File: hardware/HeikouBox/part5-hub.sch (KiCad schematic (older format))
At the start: 51 parts, among them J501 Micro_SD_Card_TFP09-2-12B, J503 PS/2, Q502 BSS138, Q503 BSS138, SW501 Left, SW502 Right, SW503 Up, SW504 Down, U501 STM32-BluePill-Socket

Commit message: BOM reduction
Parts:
- R524, R529: value 100R -> 1K
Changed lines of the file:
@@
 AR Path="/63C0F973" Ref="R?"  Part="1"
 AR Path="/646E3FCF/63C0F973" Ref="R529"  Part="1"
-F 0 "R529" V 7750 2800 50  0000 C CNN
-F 1 "100R" V 7650 2800 50  0000 C CNN
+F 0 "R529" V 7550 2800 50  0000 C CNN
+F 1 "1K" V 7650 2800 50  0000 C CNN
 F 2 "Resistor_SMD:R_0603_1608Metric_Pad0.98x0.95mm_HandSolder" V 7580 2800 50  0001 C CNN
 F 3 "~" H 7650 2800 50  0001 C CNN
@@
 AR Path="/646E3FCF/63BFC404" Ref="R524"  Part="1"
 F 0 "R524" V 7750 2600 50  0000 C CNN
-F 1 "100R" V 7650 2600 50  0000 C CNN
+F 1 "1K" V 7650 2600 50  0000 C CNN
 F 2 "Resistor_SMD:R_0603_1608Metric_Pad0.98x0.95mm_HandSolder" V 7580 2600 50  0001 C CNN
 F 3 "~" H 7650 2600 50  0001 C CNN

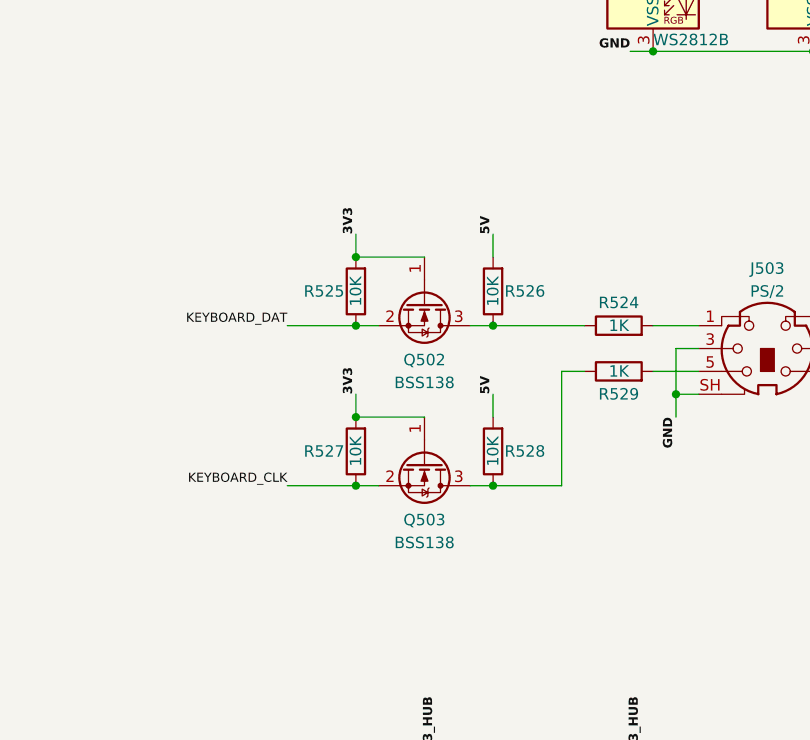
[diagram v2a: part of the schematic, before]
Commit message: Shrink VGA ladders to make space for xbus redo
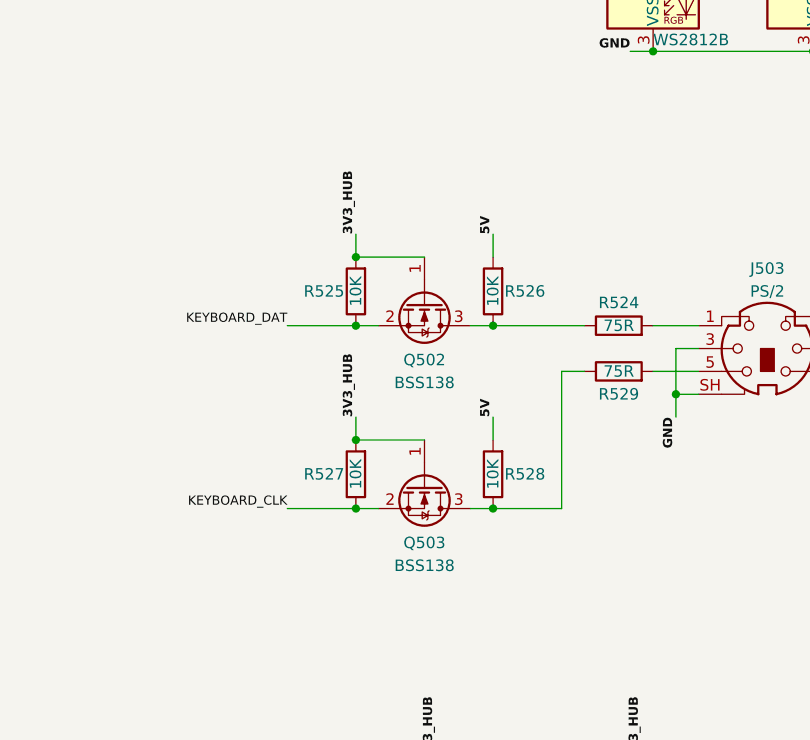
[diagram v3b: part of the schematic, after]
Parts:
- R524, R529: value 1K -> 75R
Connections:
- net 3V3: no longer Q502.1 (G), Q503.1 (G), R525.2, R527.2
- net 3V3_HUB: now also Q502.1 (G), Q503.1 (G), R525.2, R527.2
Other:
- moved on the sheet: Q503, R527, R528
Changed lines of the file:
@@
 Wire Wire Line
 	6200 2600 6500 2600
-Text Label 6200 3300 2    40   ~ 0
+Text Label 6200 3400 2    40   ~ 0
 KEYBOARD_CLK
 Wire Wire Line
@@
 Connection ~ 6500 2300
 Wire Wire Line
-	6500 3300 6200 3300
+	6500 3400 6200 3400
 Connection ~ 6500 2600
-Connection ~ 6500 3300
-Connection ~ 6500 3000
-Wire Wire Line
-	6500 3000 6500 2900
-Wire Wire Line
-	6500 3300 6600 3300
-Wire Wire Line
-	6500 3000 6800 3000
+Connection ~ 6500 3400
+Connection ~ 6500 3100
+Wire Wire Line
+	6500 3100 6500 3000
+Wire Wire Line
+	6500 3400 6600 3400
+Wire Wire Line
+	6500 3100 6800 3100
 $Comp
 L Device:R R?
 U 1 1 637DC681
-P 6500 3150
+P 6500 3250
 AR Path="/637DC681" Ref="R?"  Part="1"
 AR Path="/646E3FCF/637DC681" Ref="R527"  Part="1"
-F 0 "R527" H 6550 3150 50  0000 L CNN
-F 1 "10K" V 6500 3150 50  0000 C CNN
-F 2 "Resistor_SMD:R_0603_1608Metric_Pad0.98x0.95mm_HandSolder" V 6430 3150 50  0001 C CNN
-F 3 "~" H 6500 3150 50  0001 C CNN
-	1    6500 3150
+F 0 "R527" H 6550 3250 50  0000 L CNN
+F 1 "10K" V 6500 3250 50  0000 C CNN
+F 2 "Resistor_SMD:R_0603_1608Metric_Pad0.98x0.95mm_HandSolder" V 6430 3250 50  0001 C CNN
+F 3 "~" H 6500 3250 50  0001 C CNN
+	1    6500 3250
 	-1   0    0    1
 $EndComp
@@
 L Transistor_FET:BSS138 Q503
 U 1 1 637DC67B
-P 6800 3200
-F 0 "Q503" V 7050 3200 50  0000 C CNN
-F 1 "BSS138" V 7150 3200 50  0000 C CNN
-F 2 "Package_TO_SOT_SMD:SOT-23" H 7000 3125 50  0001 L CIN
-F 3 "https://www.onsemi.com/pub/Collateral/BSS138-D.PDF" H 6800 3200 50  0001 L CNN
-	1    6800 3200
+P 6800 3300
+F 0 "Q503" V 7050 3300 50  0000 C CNN
+F 1 "BSS138" V 7150 3300 50  0000 C CNN
+F 2 "Package_TO_SOT_SMD:SOT-23" H 7000 3225 50  0001 L CIN
+F 3 "https://www.onsemi.com/pub/Collateral/BSS138-D.PDF" H 6800 3300 50  0001 L CNN
+	1    6800 3300
 	0    1    1    0
 $EndComp
@@
 	7500 2800 7400 2800
 Wire Wire Line
-	7400 2800 7400 3300
-Connection ~ 7100 3300
-Wire Wire Line
-	7400 3300 7100 3300
-Wire Wire Line
-	7100 3300 7000 3300
+	7400 2800 7400 3400
+Connection ~ 7100 3400
+Wire Wire Line
+	7400 3400 7100 3400
+Wire Wire Line
+	7100 3400 7000 3400
 $Comp
 L Device:R R?
 U 1 1 637DC687
-P 7100 3150
+P 7100 3250
 AR Path="/637DC687" Ref="R?"  Part="1"
 AR Path="/646E3FCF/637DC687" Ref="R528"  Part="1"
-F 0 "R528" H 7050 3150 50  0000 R CNN
-F 1 "10K" V 7100 3150 50  0000 C CNN
-F 2 "Resistor_SMD:R_0603_1608Metric_Pad0.98x0.95mm_HandSolder" V 7030 3150 50  0001 C CNN
-F 3 "~" H 7100 3150 50  0001 C CNN
-	1    7100 3150
+F 0 "R528" H 7050 3250 50  0000 R CNN
+F 1 "10K" V 7100 3250 50  0000 C CNN
+F 2 "Resistor_SMD:R_0603_1608Metric_Pad0.98x0.95mm_HandSolder" V 7030 3250 50  0001 C CNN
+F 3 "~" H 7100 3250 50  0001 C CNN
+	1    7100 3250
 	-1   0    0    1
 $EndComp
@@
 $EndComp
 Wire Wire Line
-	7100 3000 7100 2900
+	7100 3100 7100 3000
 Wire Wire Line
 	7100 2300 7100 2200
@@
 AR Path="/646E3FCF/63C0F973" Ref="R529"  Part="1"
 F 0 "R529" V 7550 2800 50  0000 C CNN
-F 1 "1K" V 7650 2800 50  0000 C CNN
+F 1 "75R" V 7650 2800 50  0000 C CNN
 F 2 "Resistor_SMD:R_0603_1608Metric_Pad0.98x0.95mm_HandSolder" V 7580 2800 50  0001 C CNN
 F 3 "~" H 7650 2800 50  0001 C CNN
@@
 AR Path="/646E3FCF/63BFC404" Ref="R524"  Part="1"
 F 0 "R524" V 7750 2600 50  0000 C CNN
-F 1 "1K" V 7650 2600 50  0000 C CNN
+F 1 "75R" V 7650 2600 50  0000 C CNN
 F 2 "Resistor_SMD:R_0603_1608Metric_Pad0.98x0.95mm_HandSolder" V 7580 2600 50  0001 C CNN
 F 3 "~" H 7650 2600 50  0001 C CNN
@@
 Text Label 850  7600 0    40   ~ 8
 3V3
-Text Label 6500 2200 1    40   ~ 8
-3V3
-Text Label 6500 2900 1    40   ~ 8
-3V3
 Wire Wire Line
 	850  7500 750  7500
@@
 Text Label 850  7500 0    40   ~ 8
 5V
-Text Label 7100 2900 1    40   ~ 8
+Text Label 7100 3000 1    40   ~ 8
 5V
 Text Label 7100 2200 1    40   ~ 8
@@
 Text Notes 2750 2300 0    40   ~ 0
 to resistor fix
+Text Label 6500 3000 1    40   ~ 8
+3V3_HUB
+Text Label 6500 2200 1    40   ~ 8
+3V3_HUB
 Wire Bus Line
 	4700 6900 4700 7700

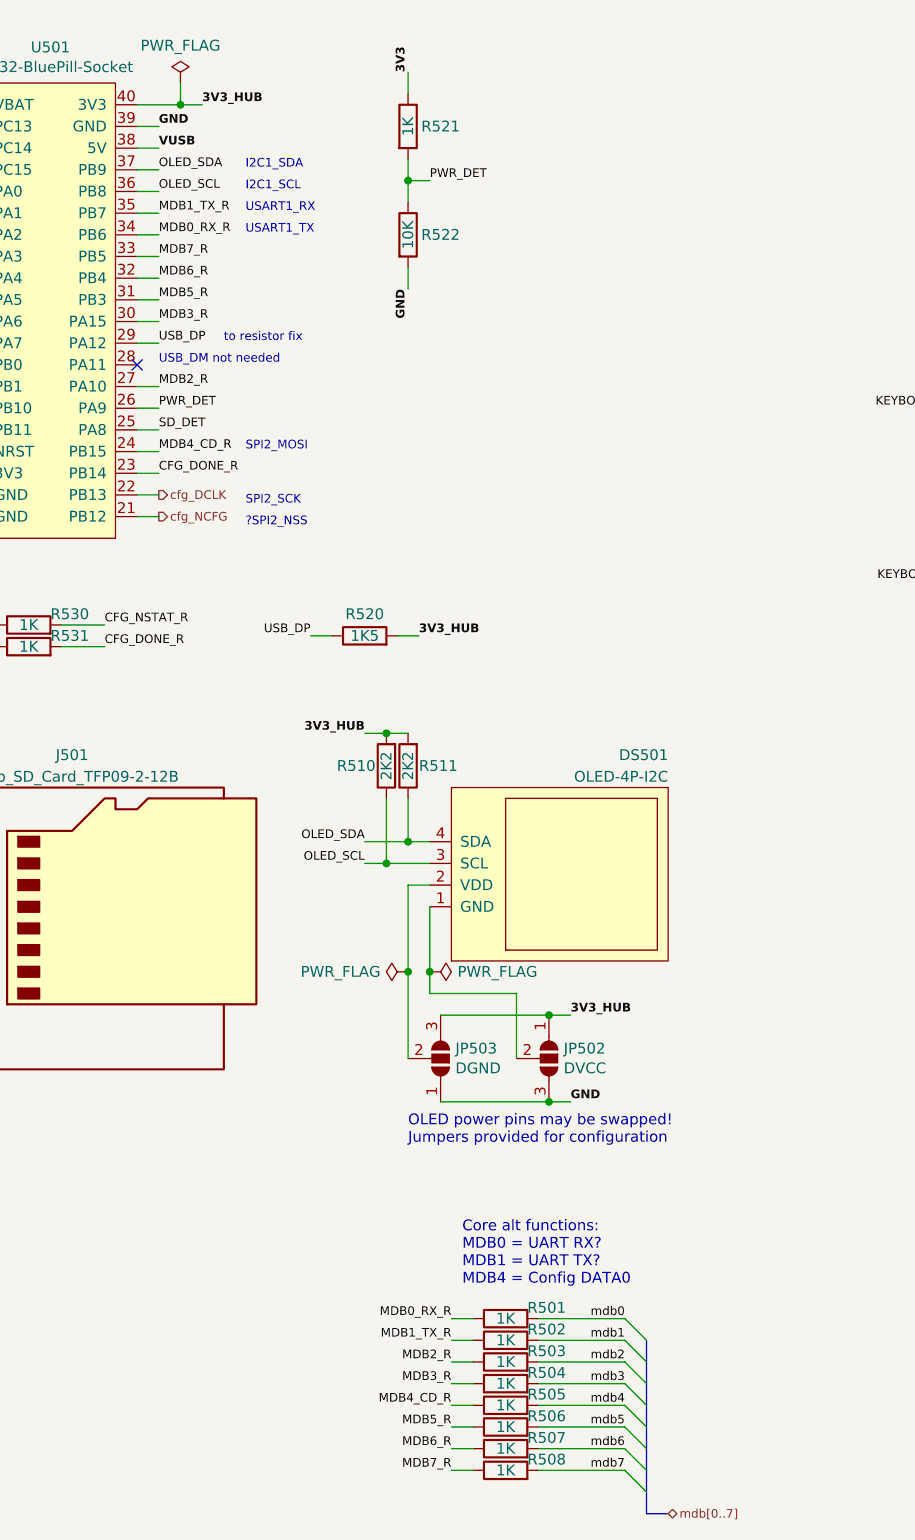
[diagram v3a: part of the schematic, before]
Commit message: Connect UART correctly, remove unused mdb connection & mdb terminology
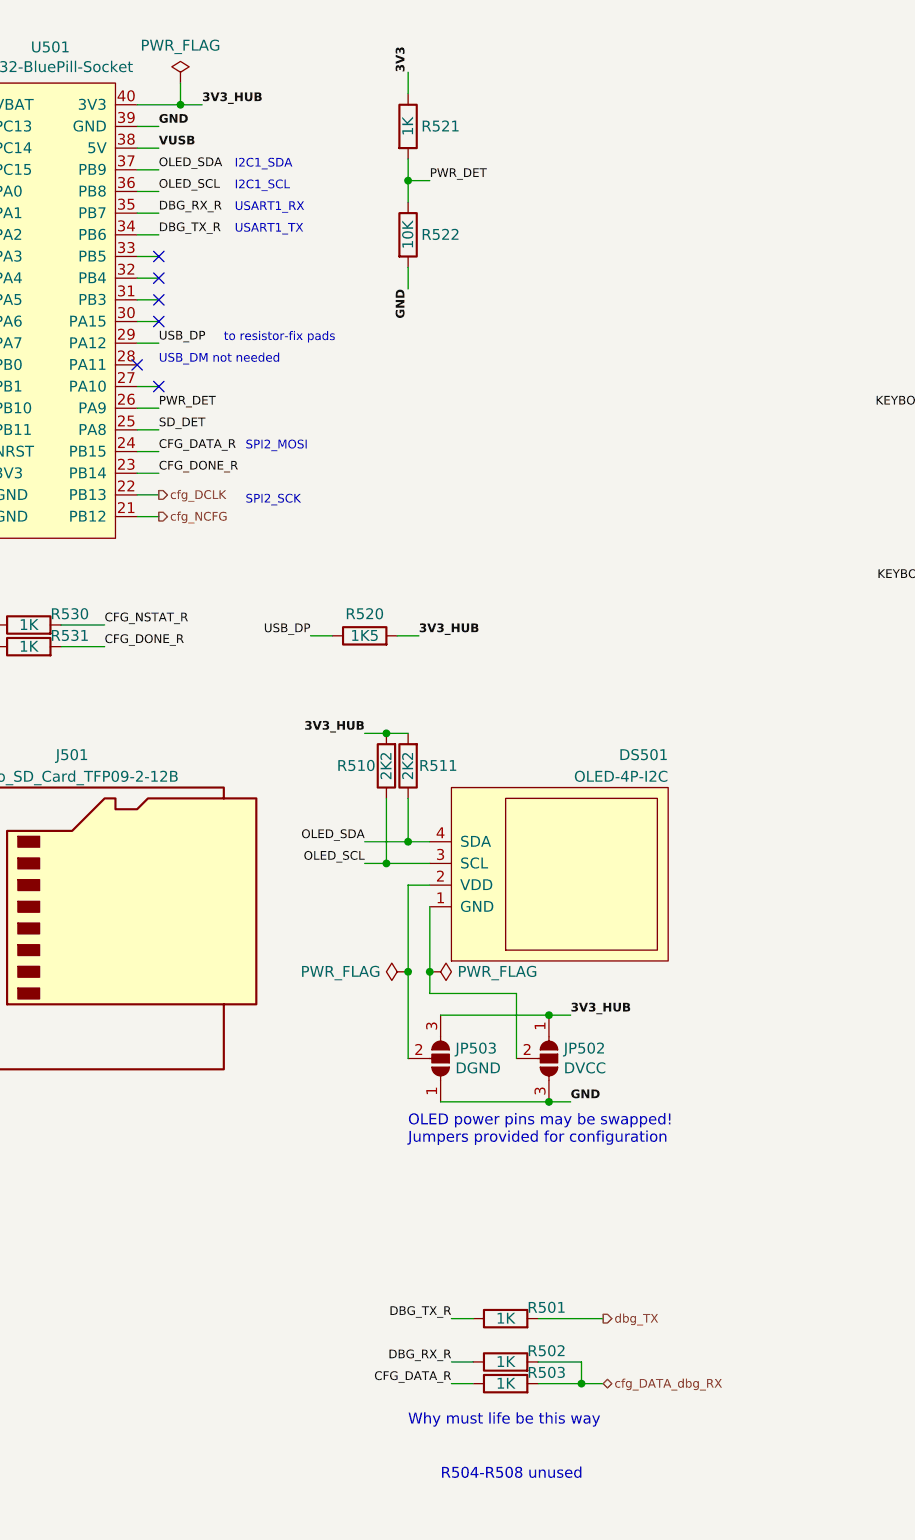
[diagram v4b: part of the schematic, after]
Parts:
- removed R504, R505, R506, R507, R508: 1K, Resistor_SMD:R_0603_1608Metric_Pad0.98x0.95mm_HandSolder, symbol Device:R
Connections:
- net mdb2 is gone; now on net cfg_DATA_dbg_RX: R503.2
- net MDB0_RX_R renamed DBG_TX_R
- net MDB1_TX_R renamed DBG_RX_R
- net MDB2_R: no longer names the net of U501.27 (PA10)
- net MDB2_R: no longer R503.1
- net MDB3_R: no longer names the net of U501.30 (PA15)
- net MDB4_CD_R renamed CFG_DATA_R
- net CFG_DATA_R: now also R503.1
- net MDB5_R: no longer names the net of U501.31 (PB3)
- net MDB6_R: no longer names the net of U501.32 (PB4)
- net MDB7_R: no longer names the net of U501.33 (PB5)
- net mdb0 renamed dbg_TX
- net mdb1 renamed cfg_DATA_dbg_RX
- no-connect marks 12 -> 17
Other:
- note added: "R504-R508 unused"
- note added: "Why must life be this way"
- note added: "to resistor-fix pads"
- note removed: "?SPI2_NSS"
- note removed: "Core alt functions:\nMDB0 = UART RX?\nMDB1 = UART TX?\nMDB4 = Config DATA0"
- note removed: "to resistor fix"
- moved on the sheet: R502, R503
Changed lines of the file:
@@
 	1100 4700 1000 4700
-Wire Wire Line
-	4200 7100 4600 7100
-$Comp
-L Device:R R?
-U 1 1 63231DEC
-P 4050 7100
-AR Path="/63231DEC" Ref="R?"  Part="1"
-AR Path="/646E3FCF/63231DEC" Ref="R504"  Part="1"
-F 0 "R504" V 4100 7000 50  0000 R CNN
-F 1 "1K" V 4050 7100 50  0000 C CNN
-F 2 "Resistor_SMD:R_0603_1608Metric_Pad0.98x0.95mm_HandSolder" V 3980 7100 50  0001 C CNN
-F 3 "~" H 4050 7100 50  0001 C CNN
-	1    4050 7100
-	0    -1   -1   0
-$EndComp
-Entry Wire Line
-	4600 7100 4700 7200
-Entry Wire Line
-	4600 7400 4700 7500
-Entry Wire Line
-	4600 7500 4700 7600
-Wire Wire Line
-	4200 7400 4600 7400
-$Comp
-L Device:R R?
-U 1 1 6323C22A
-P 4050 7400
-AR Path="/6323C22A" Ref="R?"  Part="1"
-AR Path="/646E3FCF/6323C22A" Ref="R507"  Part="1"
-F 0 "R507" V 4100 7300 50  0000 R CNN
-F 1 "1K" V 4050 7400 50  0000 C CNN
-F 2 "Resistor_SMD:R_0603_1608Metric_Pad0.98x0.95mm_HandSolder" V 3980 7400 50  0001 C CNN
-F 3 "~" H 4050 7400 50  0001 C CNN
-	1    4050 7400
-	0    -1   -1   0
-$EndComp
 Wire Wire Line
 	1100 4700 1200 4700
@@
 Text HLabel 1600 3600 0    40   Input ~ 0
 cfg_NSTAT
-Entry Wire Line
-	4600 6800 4700 6900
-Wire Wire Line
-	4200 6900 4600 6900
-Wire Wire Line
-	4200 6800 4600 6800
 $Comp
 L Device:R R?
 U 1 1 63192B13
-P 4050 6900
+P 4050 7000
 AR Path="/63192B13" Ref="R?"  Part="1"
 AR Path="/646E3FCF/63192B13" Ref="R502"  Part="1"
-F 0 "R502" V 4100 6800 50  0000 R CNN
-F 1 "1K" V 4050 6900 50  0000 C CNN
-F 2 "Resistor_SMD:R_0603_1608Metric_Pad0.98x0.95mm_HandSolder" V 3980 6900 50  0001 C CNN
-F 3 "~" H 4050 6900 50  0001 C CNN
-	1    4050 6900
+F 0 "R502" V 4100 6900 50  0000 R CNN
+F 1 "1K" V 4050 7000 50  0000 C CNN
+F 2 "Resistor_SMD:R_0603_1608Metric_Pad0.98x0.95mm_HandSolder" V 3980 7000 50  0001 C CNN
+F 3 "~" H 4050 7000 50  0001 C CNN
+	1    4050 7000
 	0    -1   -1   0
 $EndComp
@@
 	0    -1   -1   0
 $EndComp
-Entry Wire Line
-	4600 6900 4700 7000
-$Comp
-L Device:R R?
-U 1 1 632371E8
-P 4050 7300
-AR Path="/632371E8" Ref="R?"  Part="1"
-AR Path="/646E3FCF/632371E8" Ref="R506"  Part="1"
-F 0 "R506" V 4100 7200 50  0000 R CNN
-F 1 "1K" V 4050 7300 50  0000 C CNN
-F 2 "Resistor_SMD:R_0603_1608Metric_Pad0.98x0.95mm_HandSolder" V 3980 7300 50  0001 C CNN
-F 3 "~" H 4050 7300 50  0001 C CNN
-	1    4050 7300
-	0    -1   -1   0
-$EndComp
-Wire Wire Line
-	4200 7300 4600 7300
-Entry Wire Line
-	4600 7300 4700 7400
-Entry Wire Line
-	4600 7200 4700 7300
-Wire Wire Line
-	4200 7200 4600 7200
-Entry Wire Line
-	4600 7000 4700 7100
-Wire Bus Line
-	4700 7700 4800 7700
-Wire Wire Line
-	4200 7000 4600 7000
+Wire Wire Line
+	4200 7100 4400 7100
 $Comp
 L Device:R R?
 U 1 1 63231DF2
-P 4050 7000
+P 4050 7100
 AR Path="/63231DF2" Ref="R?"  Part="1"
 AR Path="/646E3FCF/63231DF2" Ref="R503"  Part="1"
-F 0 "R503" V 4100 6900 50  0000 R CNN
-F 1 "1K" V 4050 7000 50  0000 C CNN
-F 2 "Resistor_SMD:R_0603_1608Metric_Pad0.98x0.95mm_HandSolder" V 3980 7000 50  0001 C CNN
-F 3 "~" H 4050 7000 50  0001 C CNN
-	1    4050 7000
-	0    -1   -1   0
-$EndComp
-$Comp
-L Device:R R?
-U 1 1 632371EE
-P 4050 7200
-AR Path="/632371EE" Ref="R?"  Part="1"
-AR Path="/646E3FCF/632371EE" Ref="R505"  Part="1"
-F 0 "R505" V 4100 7100 50  0000 R CNN
-F 1 "1K" V 4050 7200 50  0000 C CNN
-F 2 "Resistor_SMD:R_0603_1608Metric_Pad0.98x0.95mm_HandSolder" V 3980 7200 50  0001 C CNN
-F 3 "~" H 4050 7200 50  0001 C CNN
-	1    4050 7200
+F 0 "R503" V 4100 7000 50  0000 R CNN
+F 1 "1K" V 4050 7100 50  0000 C CNN
+F 2 "Resistor_SMD:R_0603_1608Metric_Pad0.98x0.95mm_HandSolder" V 3980 7100 50  0001 C CNN
+F 3 "~" H 4050 7100 50  0001 C CNN
+	1    4050 7100
 	0    -1   -1   0
 $EndComp
 Text HLabel 2450 3000 2    40   Output ~ 0
 cfg_DCLK
-Text HLabel 4800 7700 2    40   BiDi ~ 0
-mdb[0..7]
 $Comp
 L Device:R R?
@@
 Wire Wire Line
 	2200 3600 2000 3600
-Text Label 4600 7200 2    40   ~ 0
-mdb4
-Text Label 4600 7000 2    40   ~ 0
-mdb2
-Text Label 4600 7300 2    40   ~ 0
-mdb5
-Text Label 4600 6900 2    40   ~ 0
-mdb1
-Text Label 4600 6800 2    40   ~ 0
-mdb0
-Text Label 4600 7400 2    40   ~ 0
-mdb6
-Text Label 4600 7500 2    40   ~ 0
-mdb7
-Text Label 4600 7100 2    40   ~ 0
-mdb3
 Wire Wire Line
 	3400 4700 3500 4700
-Wire Wire Line
-	4200 7500 4600 7500
-$Comp
-L Device:R R?
-U 1 1 6323C224
-P 4050 7500
-AR Path="/6323C224" Ref="R?"  Part="1"
-AR Path="/646E3FCF/6323C224" Ref="R508"  Part="1"
-F 0 "R508" V 4100 7400 50  0000 R CNN
-F 1 "1K" V 4050 7500 50  0000 C CNN
-F 2 "Resistor_SMD:R_0603_1608Metric_Pad0.98x0.95mm_HandSolder" V 3980 7500 50  0001 C CNN
-F 3 "~" H 4050 7500 50  0001 C CNN
-	1    4050 7500
-	0    -1   -1   0
-$EndComp
 Wire Wire Line
 	7700 800  7800 800
@@
 Text Label 1000 4800 2    40   ~ 0
 SD_MOSI
-Text Label 3800 6900 2    40   ~ 0
-MDB1_TX_R
-Wire Wire Line
-	3800 6900 3900 6900
+Text Label 3800 7000 2    40   ~ 0
+DBG_RX_R
+Wire Wire Line
+	3800 7000 3900 7000
 Text Label 3800 6800 2    40   ~ 0
-MDB0_RX_R
+DBG_TX_R
 Wire Wire Line
 	3800 6800 3900 6800
-Text Label 3800 7200 2    40   ~ 0
-MDB4_CD_R
-Wire Wire Line
-	3800 7200 3900 7200
-Text Label 3800 7000 2    40   ~ 0
-MDB2_R
-Wire Wire Line
-	3800 7000 3900 7000
 Text Label 3800 7100 2    40   ~ 0
-MDB3_R
-Wire Wire Line
-	3800 7100 3900 7100
-Text Notes 3850 6650 0    50   ~ 0
-Core alt functions:\nMDB0 = UART RX?\nMDB1 = UART TX?\nMDB4 = Config DATA0
-Text Label 3800 7300 2    40   ~ 0
-MDB5_R
-Wire Wire Line
-	3800 7300 3900 7300
-Text Label 3800 7400 2    40   ~ 0
-MDB6_R
-Wire Wire Line
-	3800 7400 3900 7400
-Text Label 3800 7500 2    40   ~ 0
-MDB7_R
-Wire Wire Line
-	3800 7500 3900 7500
+CFG_DATA_R
 Wire Wire Line
 	6950 4900 6850 4900
@@
 Wire Wire Line
 	2450 2200 2350 2200
-Text Label 2450 2200 0    40   ~ 0
-MDB3_R
 NoConn ~ 2350 2400
 Text Notes 1150 2000 2    40   ~ 0
@@
 	2450 2800 2350 2800
 Text Label 2450 2800 0    40   ~ 0
-MDB4_CD_R
+CFG_DATA_R
 Text Label 2450 2900 0    40   ~ 0
 CFG_DONE_R
@@
 Wire Wire Line
 	2450 3000 2350 3000
-Text Notes 2850 3150 0    40   ~ 0
-?SPI2_NSS
 Wire Wire Line
 	2450 3100 2350 3100
@@
 Wire Wire Line
 	1450 2500 1550 2500
-Text Notes 2850 1600 0    40   ~ 0
+Text Notes 2800 1600 0    40   ~ 0
 I2C1_SCL
-Text Notes 2850 1500 0    40   ~ 0
+Text Notes 2800 1500 0    40   ~ 0
 I2C1_SDA
 Wire Wire Line
@@
 Wire Wire Line
 	2450 1600 2350 1600
-Text Notes 2850 1800 0    40   ~ 0
+Text Notes 2800 1800 0    40   ~ 0
 USART1_TX
-Text Notes 2850 1700 0    40   ~ 0
+Text Notes 2800 1700 0    40   ~ 0
 USART1_RX
 Text Label 2450 1700 0    40   ~ 0
-MDB1_TX_R
+DBG_RX_R
 Wire Wire Line
 	2450 1700 2350 1700
 Text Label 2450 1800 0    40   ~ 0
-MDB0_RX_R
+DBG_TX_R
 Wire Wire Line
 	2450 1800 2350 1800
 Wire Wire Line
 	2450 2100 2350 2100
-Text Label 2450 2100 0    40   ~ 0
-MDB5_R
 Wire Wire Line
 	2450 1900 2350 1900
-Text Label 2450 1900 0    40   ~ 0
-MDB7_R
 Wire Wire Line
 	2450 2000 2350 2000
-Text Label 2450 2000 0    40   ~ 0
-MDB6_R
 Wire Wire Line
 	1450 2600 1550 2600
@@
 Wire Wire Line
 	2450 2500 2350 2500
-Text Label 2450 2500 0    40   ~ 0
-MDB2_R
 Wire Wire Line
 	2450 2700 2350 2700
@@
 $EndComp
 Text Notes 2750 2300 0    40   ~ 0
-to resistor fix
+to resistor-fix pads
 Text Label 6500 3000 1    40   ~ 8
 3V3_HUB
 Text Label 6500 2200 1    40   ~ 8
 3V3_HUB
-Wire Bus Line
-	4700 6900 4700 7700
+NoConn ~ 2450 1900
+NoConn ~ 2450 2000
+NoConn ~ 2450 2100
+NoConn ~ 2450 2200
+NoConn ~ 2450 2500
+Wire Wire Line
+	3900 7100 3800 7100
+Wire Wire Line
+	4200 7000 4400 7000
+Wire Wire Line
+	4400 7000 4400 7100
+Text Notes 3600 7300 0    50   ~ 0
+Why must life be this way
+Text HLabel 4500 6800 2    40   Output ~ 0
+dbg_TX
+Wire Wire Line
+	4500 6800 4200 6800
+Text HLabel 4500 7100 2    40   BiDi ~ 0
+cfg_DATA_dbg_RX
+Wire Wire Line
+	4500 7100 4400 7100
+Connection ~ 4400 7100
+Text Notes 3750 7550 0    50   ~ 0
+R504-R508 unused
 $EndSCHEMATC
